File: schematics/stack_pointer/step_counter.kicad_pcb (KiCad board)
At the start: 2 copper layers, 100 x 91 mm, 17 parts, among them U1 74HC00, U2 74HC193, U3 74HC193, U4 74HC193, U5 74HC193, U6 74HC245, U7 74HC245

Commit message: silklayer check
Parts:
- moved C3 7.06 mm to (121.0, 44.2), turned to 0 degrees
- moved C2 6.66 mm to (121.0, 60.2), turned to 0 degrees
- moved C6 2.64 mm to (150.8, 88.2)
- moved kibuzzard-6911C575 2.35 mm to (119.9, 79.8)
- moved C5 1.55 mm to (166.7, 44.2)
- moved C8 0.90 mm to (192.5, 114.1)
- moved C7 0.55 mm to (156.2, 104.5)
- moved C4 0.39 mm to (166.7, 60.2)
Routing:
- net /DL3: track 54.0 -> 55.3 mm
- net /DL2: track 53.8 -> 54.9 mm
- net VCC: track 59.3 -> 60.0 mm
- net /LSPH: track 84.9 -> 84.4 mm

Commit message: power change
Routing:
- net GND: track 127.8 -> 191.7 mm
- net VCC: track 60.0 -> 82.6 mm, vias 1 -> 7

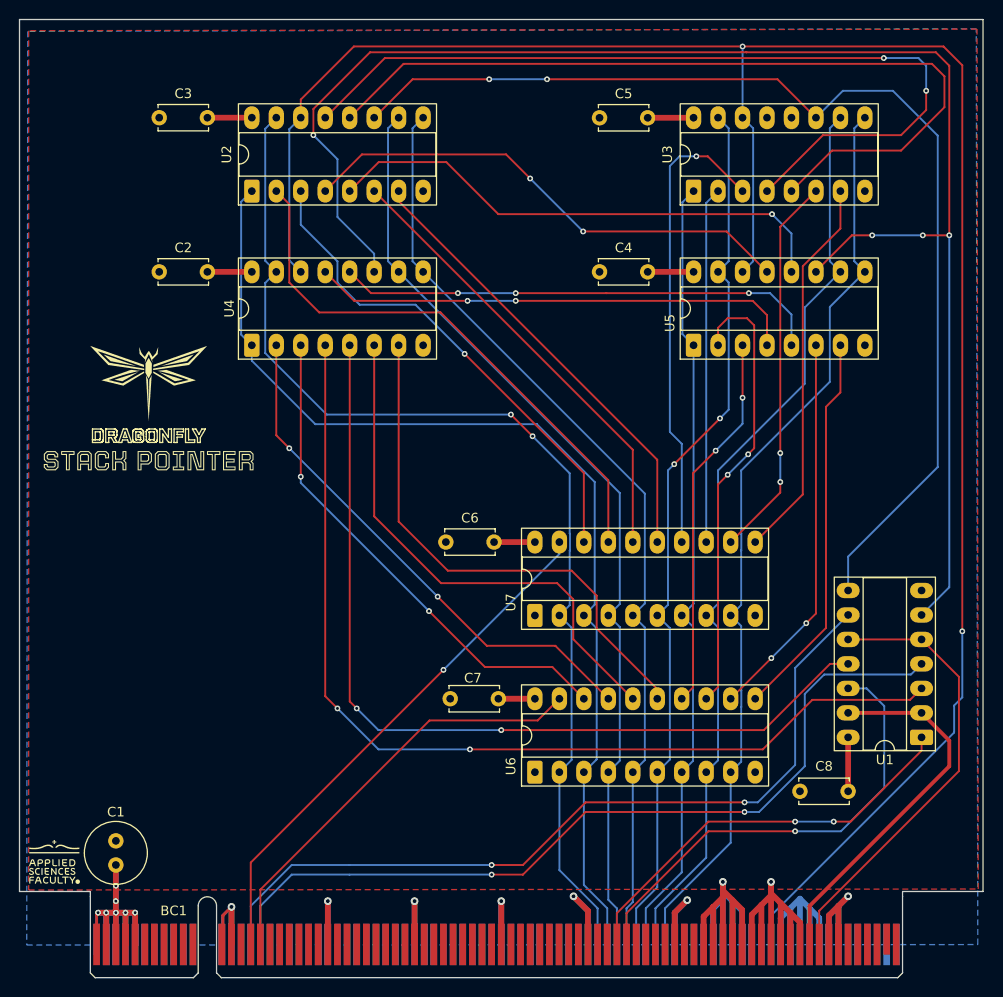
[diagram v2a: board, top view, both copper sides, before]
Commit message: fix: removed in control pins daisy chains
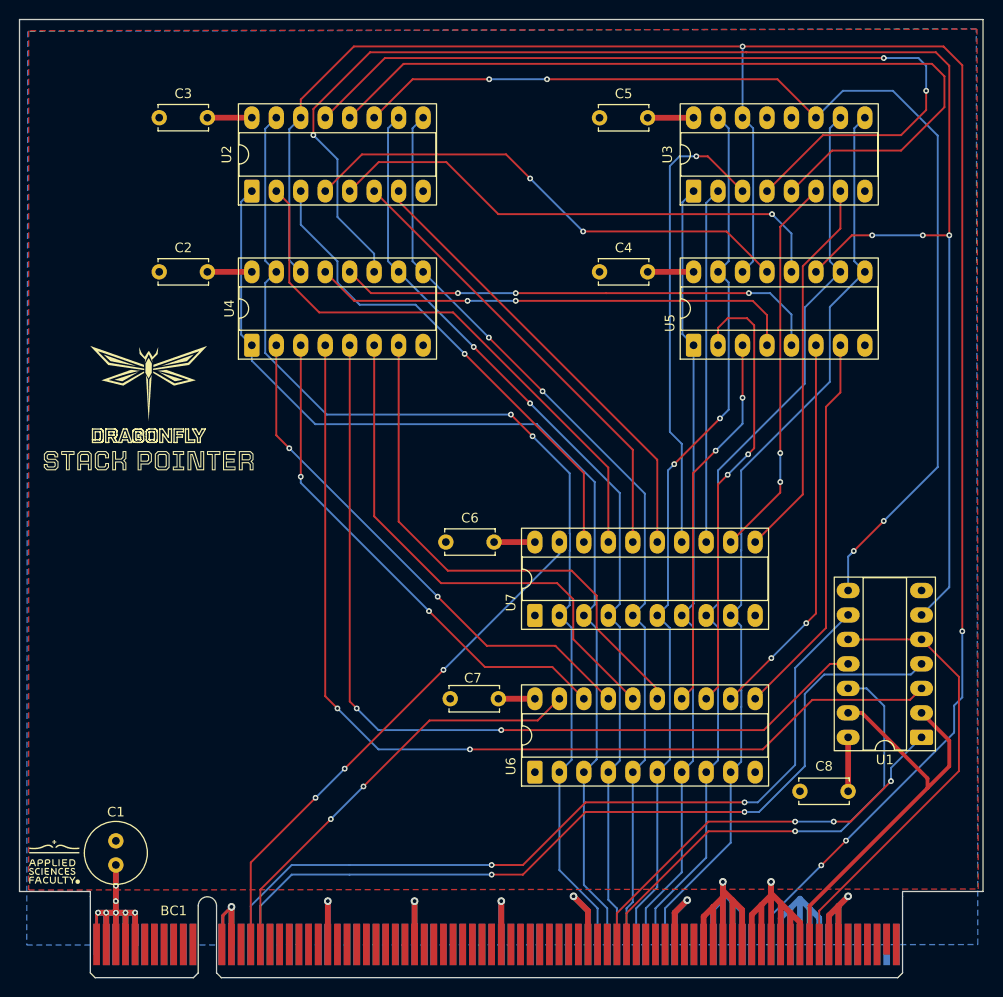
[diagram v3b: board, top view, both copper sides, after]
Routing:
- net /~{CLK}: track 38.9 -> 43.3 mm
- net /DH1: track 58.1 -> 58.8 mm
- net /RESET: vias 2 -> 4
- net /~{RSPL}: vias 0 -> 2
- net /~{RSPH}: vias 1 -> 3
- net /SPDEC: vias 2 -> 3
- net /Ph: vias 2 -> 4
- net /DATA3: vias 0 -> 2
- net /DATA2: vias 0 -> 2
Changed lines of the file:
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@@
 	(segment
 		(start 131.5 124.3)
-		(end 149.05 106.75)
+		(end 138.8125 116.9875)
 		(width 0.2)
 		(layer "F.Cu")
@@
 	)
 	(segment
+		(start 142.2 113.6)
+		(end 149.05 106.75)
+		(width 0.2)
+		(layer "F.Cu")
+		(net 3)
+	)
+	(via
+		(at 142.2 113.6)
+		(size 0.6)
+		(drill 0.3)
+		(layers "F.Cu" "B.Cu")
+		(net 3)
+	)
+	(via
+		(at 138.8125 116.9875)
+		(size 0.6)
+		(drill 0.3)
+		(layers "F.Cu" "B.Cu")
+		(net 3)
+	)
+	(segment
+		(start 138.8125 116.9875)
+		(end 142.2 113.6)
+		(width 0.2)
+		(layer "B.Cu")
+		(net 3)
+	)
+	(segment
 		(start 150.5 101.5)
+		(end 140.25 111.75)
+		(width 0.2)
+		(layer "F.Cu")
+		(net 4)
+	)
+	(segment
+		(start 137.225 114.775)
 		(end 130.5 121.5)
 		(width 0.2)
@@
 		(net 4)
 	)
+	(via
+		(at 140.25 111.75)
+		(size 0.6)
+		(drill 0.3)
+		(layers "F.Cu" "B.Cu")
+		(net 4)
+	)
+	(via
+		(at 137.225 114.775)
+		(size 0.6)
+		(drill 0.3)
+		(layers "F.Cu" "B.Cu")
+		(net 4)
+	)
 	(segment
 		(start 162.532254 89.467746)
@@
 	)
 	(segment
+		(start 137.225 114.775)
+		(end 140.25 111.75)
+		(width 0.2)
+		(layer "B.Cu")
+		(net 4)
+	)
+	(segment
 		(start 150.5 101.5)
 		(end 162.532254 89.467746)
@@
 	)
 	(segment
+		(start 189.7125 121.7875)
+		(end 192.275 119.225)
+		(width 0.2)
+		(layer "F.Cu")
+		(net 6)
+	)
+	(segment
 		(start 141.2 36.8)
 		(end 135.69 42.31)
@@
 	)
 	(via
+		(at 192.275 119.225)
+		(size 0.6)
+		(drill 0.3)
+		(layers "F.Cu" "B.Cu")
+		(net 6)
+	)
+	(via
 		(at 181.545513 36.801)
 		(size 0.6)
@@
 		(net 6)
 	)
+	(via
+		(at 189.7125 121.7875)
+		(size 0.6)
+		(drill 0.3)
+		(layers "F.Cu" "B.Cu")
+		(net 6)
+	)
 	(segment
 		(start 182.641 59.089)
@@
 	)
 	(segment
-		(start 203.5 108)
+		(start 189.7125 121.7875)
 		(end 184.5 127)
 		(width 0.2)
@@
 	)
 	(segment
+		(start 203.5 108)
+		(end 192.275 119.225)
+		(width 0.2)
+		(layer "B.Cu")
+		(net 6)
+	)
+	(segment
 		(start 181.54 36.84)
 		(end 181.54 44.19)
@@
 	)
 	(segment
-		(start 200.12 109.88)
-		(end 200.12 108.5)
-		(width 0.2)
-		(layer "F.Cu")
-		(net 9)
-	)
-	(segment
 		(start 192.75 117.25)
-		(end 200.12 109.88)
+		(end 196.95 113.05)
 		(width 0.2)
 		(layer "F.Cu")
@@
 	)
 	(via
+		(at 196.95 113.05)
+		(size 0.6)
+		(drill 0.3)
+		(layers "F.Cu" "B.Cu")
+		(net 9)
+	)
+	(via
 		(at 191 117.25)
 		(size 0.6)
@@
 	)
 	(segment
+		(start 196.95 111.67)
+		(end 200.12 108.5)
+		(width 0.2)
+		(layer "B.Cu")
+		(net 9)
+	)
+	(segment
+		(start 196.95 113.05)
+		(end 196.95 111.67)
+		(width 0.2)
+		(layer "B.Cu")
+		(net 9)
+	)
+	(segment
 		(start 198 47.6)
 		(end 202.5 43.1)
@@
 	)
 	(segment
-		(start 137.6 64.4)
-		(end 150.2 64.4)
+		(start 133.15 51.81)
+		(end 134.5 53.16)
 		(width 0.2)
 		(layer "F.Cu")
@@
 	)
 	(segment
-		(start 167.612254 81.812254)
+		(start 167.612254 80.512254)
 		(end 167.612254 88.234777)
 		(width 0.2)
@@
 	)
 	(segment
-		(start 150.2 64.4)
-		(end 167.612254 81.812254)
+		(start 134.5 61.3)
+		(end 137.6 64.4)
 		(width 0.2)
 		(layer "F.Cu")
@@
 	)
 	(segment
-		(start 133.15 51.81)
-		(end 134.5 53.16)
+		(start 134.5 53.16)
+		(end 134.5 61.3)
 		(width 0.2)
 		(layer "F.Cu")
@@
 	)
 	(segment
-		(start 134.5 53.16)
-		(end 134.5 61.3)
+		(start 151.5 64.4)
+		(end 167.612254 80.512254)
 		(width 0.2)
 		(layer "F.Cu")
@@
 	)
 	(segment
-		(start 134.5 61.3)
-		(end 137.6 64.4)
+		(start 137.6 64.4)
+		(end 151.5 64.4)
 		(width 0.2)
 		(layer "F.Cu")
@@
 	)
 	(segment
+		(start 159.4925 73.8325)
+		(end 153.6425 67.9825)
+		(width 0.2)
+		(layer "F.Cu")
+		(net 64)
+	)
+	(via
+		(at 153.6425 67.9825)
+		(size 0.6)
+		(drill 0.3)
+		(layers "F.Cu" "B.Cu")
+		(net 64)
+	)
+	(via
+		(at 159.4925 73.8325)
+		(size 0.6)
+		(drill 0.3)
+		(layers "F.Cu" "B.Cu")
+		(net 64)
+	)
+	(segment
 		(start 144.749 59.089)
 		(end 144.749 45.291)
@@
 	)
 	(segment
+		(start 153.6425 67.9825)
+		(end 145.85 60.19)
+		(width 0.2)
+		(layer "B.Cu")
+		(net 64)
+	)
+	(segment
 		(start 167.612254 112.115735)
 		(end 168.8 110.927989)
@@
 	(segment
 		(start 168.8 83.14)
-		(end 145.85 60.19)
+		(end 159.4925 73.8325)
 		(width 0.2)
 		(layer "B.Cu")
@@
 	)
 	(segment
+		(start 160.7875 72.5875)
+		(end 155.2125 67.0125)
+		(width 0.2)
+		(layer "F.Cu")
+		(net 65)
+	)
+	(via
+		(at 155.2125 67.0125)
+		(size 0.6)
+		(drill 0.3)
+		(layers "F.Cu" "B.Cu")
+		(net 65)
+	)
+	(via
+		(at 160.7875 72.5875)
+		(size 0.6)
+		(drill 0.3)
+		(layers "F.Cu" "B.Cu")
+		(net 65)
+	)
+	(segment
 		(start 148.39 60.19)
 		(end 147.289 59.089)
@@
 	)
 	(segment
+		(start 155.2125 67.0125)
+		(end 148.39 60.19)
+		(width 0.2)
+		(layer "B.Cu")
+		(net 65)
+	)
+	(segment
 		(start 171.4 94.607031)
 		(end 171.4 83.2)
@@
 	(segment
 		(start 171.4 83.2)
-		(end 148.39 60.19)
+		(end 160.7875 72.5875)
 		(width 0.2)
 		(layer "B.Cu")
@@
 	)
 	(segment
-		(start 200.12 105.96)
+		(start 193.935 105.96)
 		(end 192.5 105.96)
 		(width 0.4)
@@
 	)
 	(segment
-		(start 188.5 126)
+		(start 200.7375 113.7625)
 		(end 203 111.5)
 		(width 0.4)
@@
 	)
 	(segment
+		(start 188.5 126)
+		(end 200.7375 113.7625)
+		(width 0.4)
+		(layer "F.Cu")
+		(net 111)
+	)
+	(segment
+		(start 200.7375 112.7625)
+		(end 193.935 105.96)
+		(width 0.4)
+		(layer "F.Cu")
+		(net 111)
+	)
+	(segment
 		(start 188.5 130)
 		(end 188.5 126)
@@
 	)
 	(segment
+		(start 200.7375 113.7625)
+		(end 200.7375 112.7625)
+		(width 0.4)
+		(layer "F.Cu")
+		(net 111)
+	)
+	(segment
 		(start 165.25 116.25)
 		(end 181.75 116.25)
@@
 	)
 	(segment
+		(start 193.0875 89.1625)
+		(end 196.2 86.05)
+		(width 0.2)
+		(layer "F.Cu")
+		(net 113)
+	)
+	(segment
 		(start 185.17 40.2)
 		(end 161.25 40.2)
@@
 	)
 	(via
+		(at 193.0875 89.1625)
+		(size 0.6)
+		(drill 0.3)
+		(layers "F.Cu" "B.Cu")
+		(net 113)
+	)
+	(via
 		(at 161.25 40.2)
 		(size 0.6)
@@
 		(net 113)
 	)
+	(via
+		(at 196.2 86.05)
+		(size 0.6)
+		(drill 0.3)
+		(layers "F.Cu" "B.Cu")
+		(net 113)
+	)
+	(segment
+		(start 192.85 89.4)
+		(end 192.5 89.75)
+		(width 0.2)
+		(layer "B.Cu")
+		(net 113)
+	)
 	(segment
 		(start 189.16 44.19)
@@
 	(segment
 		(start 201.8 80.45)
-		(end 192.5 89.75)
+		(end 196.2 86.05)
+		(width 0.2)
+		(layer "B.Cu")
+		(net 113)
+	)
+	(segment
+		(start 193.0875 89.1625)
+		(end 192.85 89.4)
+		(width 0.2)
+		(layer "B.Cu")
+		(net 113)
+	)
+	(segment
+		(start 192.5 89.75)
+		(end 192.5 93.26)
 		(width 0.2)
 		(layer "B.Cu")
@@
 	)
 	(segment
-		(start 192.5 89.75)
-		(end 192.5 93.26)
-		(width 0.2)
-		(layer "B.Cu")
-		(net 113)
-	)
-	(segment
 		(start 198.931 104.609)
 		(end 188.793519 104.609)
@@
 		(priority 1)
 		(connect_pads
-			(clearance 0.25)
+			(clearance 0.35)
 		)
 		(min_thickness 0.25)
@@
 		(hatch edge 0.5)
 		(connect_pads
-			(clearance 0.25)
+			(clearance 0.35)
 		)
 		(min_thickness 0.25)

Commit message: update pc and sp
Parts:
- removed kibuzzard-6911C575: G***, kibuzzard-6911C575
- added kibuzzard-6911BE41: G***, kibuzzard-6911BE41, F.Cu at (190.2, 50.2)
- moved U3 66.7 mm to (125.3, 94.6)
- moved C5 66.5 mm to (115.8, 87.0)
- moved C3 61.1 mm to (111.0, 104.5)
- moved C2 53.4 mm to (150.8, 104.5)
- moved C7 47.2 mm to (120.8, 73.4)
- moved U7 43.0 mm to (120.2, 112.1)
- moved U4 37.4 mm to (165.2, 82.0)
- moved U5 32.2 mm to (165.2, 98.0)
- moved C4 32.1 mm to (155.7, 90.4)
- moved U2 29.7 mm to (125.2, 81.0)
- moved C6 14.7 mm to (155.8, 74.4)
- moved C8 0.95 mm to (192.5, 115.0)
- moved C1 0.24 mm to (116.5, 122.0)
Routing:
- net /Pl: track 162.2 -> 47.3 mm, vias 4 -> 1
- net /DATA2: track 98.1 -> 195.9 mm, vias 2 -> 3
- net Net-(U2-~{BO}): track 89.9 -> 22.2 mm, vias 2 -> 0
- net Net-(U2-~{CO}): track 87.3 -> 22.3 mm
- net /CPu: track 92.8 -> 31.9 mm, vias 2 -> 3
- net /CPd: track 103.2 -> 48.5 mm, vias 2 -> 8
- net /DATA3: track 98.1 -> 147.4 mm, vias 2 -> 5
- net /DH4: track 49.0 -> 12.0 mm, vias 1 -> 0
- net /DH1: track 58.8 -> 24.4 mm
- net /RESET: track 214.4 -> 181.3 mm
- net /DL6: track 40.4 -> 7.51 mm, vias 2 -> 0
- net /DL7: track 40.4 -> 7.51 mm
- net /DL5: track 47.1 -> 15.0 mm, vias 2 -> 0
- net /DATA0: track 114.7 -> 146.1 mm, vias 2 -> 3
- net /DATA5: track 82.2 -> 113.0 mm, vias 0 -> 3
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
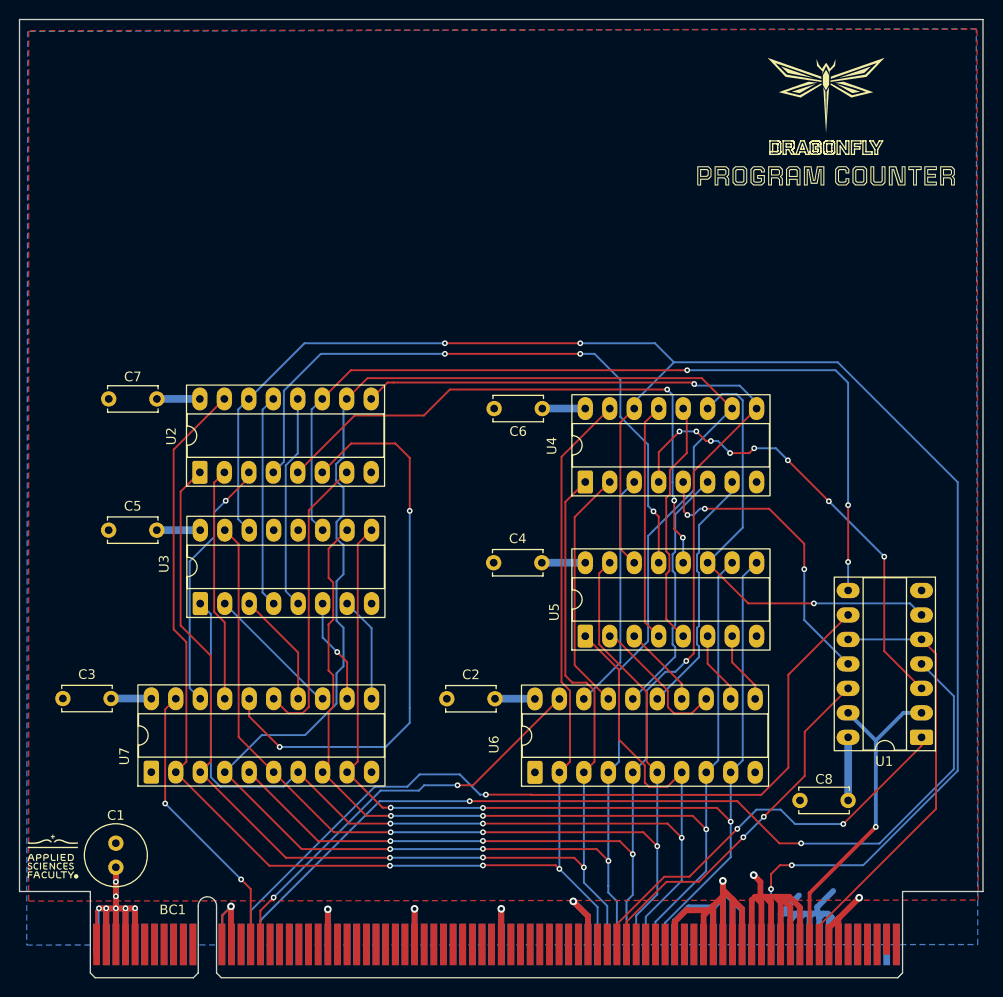
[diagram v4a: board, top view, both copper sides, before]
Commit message: test points sp and pc
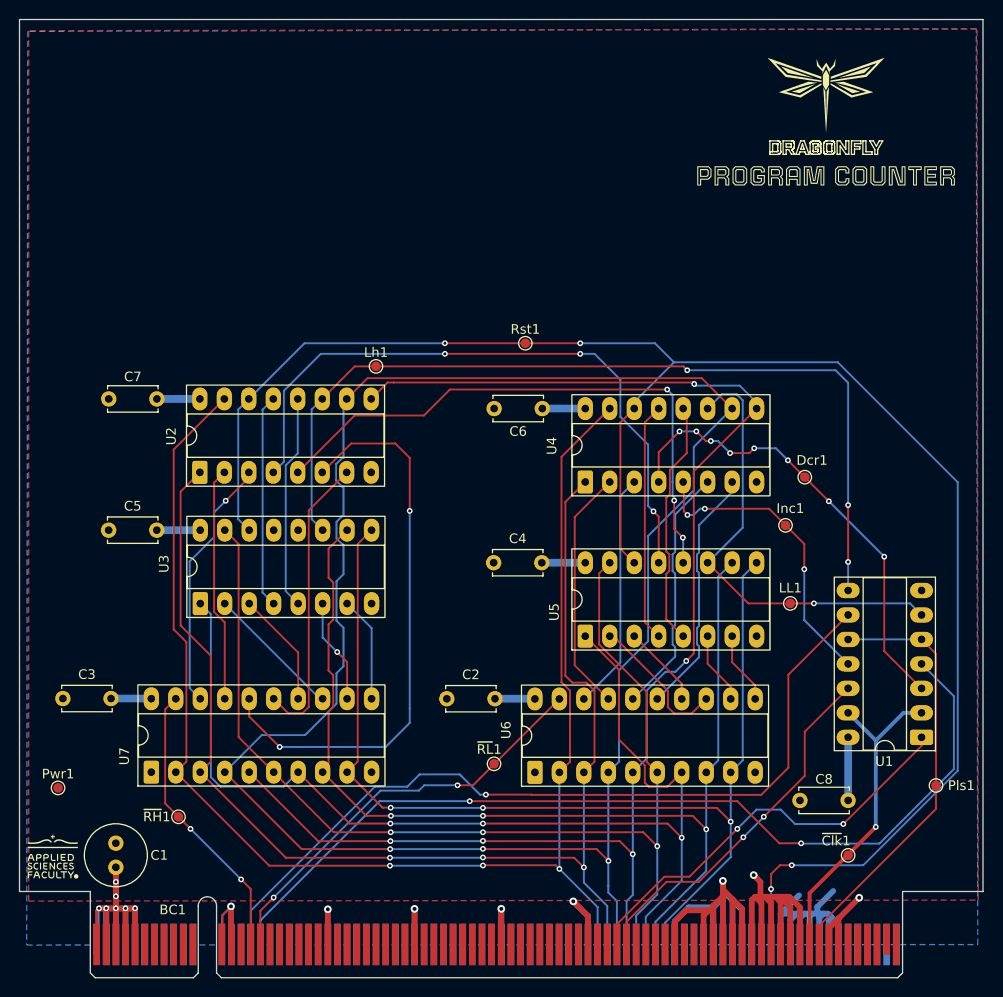
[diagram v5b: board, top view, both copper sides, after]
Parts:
- added Dcr1: Decrement, TestPoint:TestPoint_Pad_D1.0mm, F.Cu at (188.0, 81.5)
- added Inc1: Increment, TestPoint:TestPoint_Pad_D1.0mm, F.Cu at (186.0, 86.5)
- added LL1: LoadLow, TestPoint:TestPoint_Pad_D1.0mm, F.Cu at (186.5, 94.6)
- added Lh1: LoadHigh, TestPoint:TestPoint_Pad_D1.0mm, F.Cu at (143.5, 70.0)
- added Pls1: Pulse, TestPoint:TestPoint_Pad_D1.0mm, F.Cu at (201.6, 113.5)
- added Pwr1: Power, TestPoint:TestPoint_Pad_D1.0mm, F.Cu at (110.5, 113.8)
- added Rst1: Reset, TestPoint:TestPoint_Pad_D1.0mm, F.Cu at (159.0, 67.6)
- added ~{Clk}1: ~{Clock}, TestPoint:TestPoint_Pad_D1.0mm, F.Cu at (192.5, 120.8)
- added ~{RH}1: ~{ReadHigh}, TestPoint:TestPoint_Pad_D1.0mm, F.Cu at (123.0, 116.8)
- added ~{RL}1: ~{ReadLow}, TestPoint:TestPoint_Pad_D1.0mm, F.Cu at (155.8, 111.2)

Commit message: fix
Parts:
- added kibuzzard-691DD7C3: G***, kibuzzard-691DD7C3, F.Cu at (115.0, 37.4)
